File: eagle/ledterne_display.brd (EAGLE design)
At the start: 15 x 15 mm, 5 parts

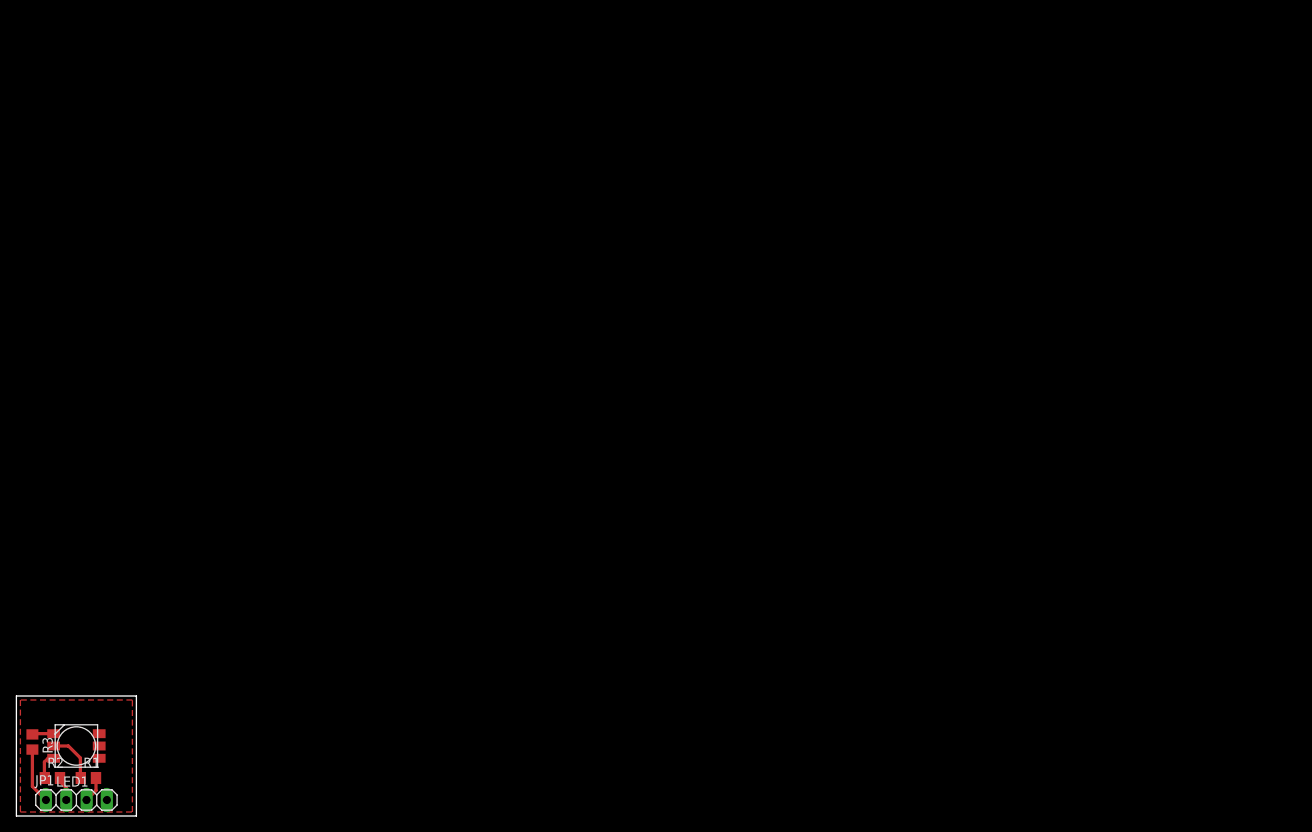
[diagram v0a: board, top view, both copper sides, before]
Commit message: Add layout versions for printing a complete Eurocard board
The display board also has Yo's entirely unrelated layout on the
same Eurocard.
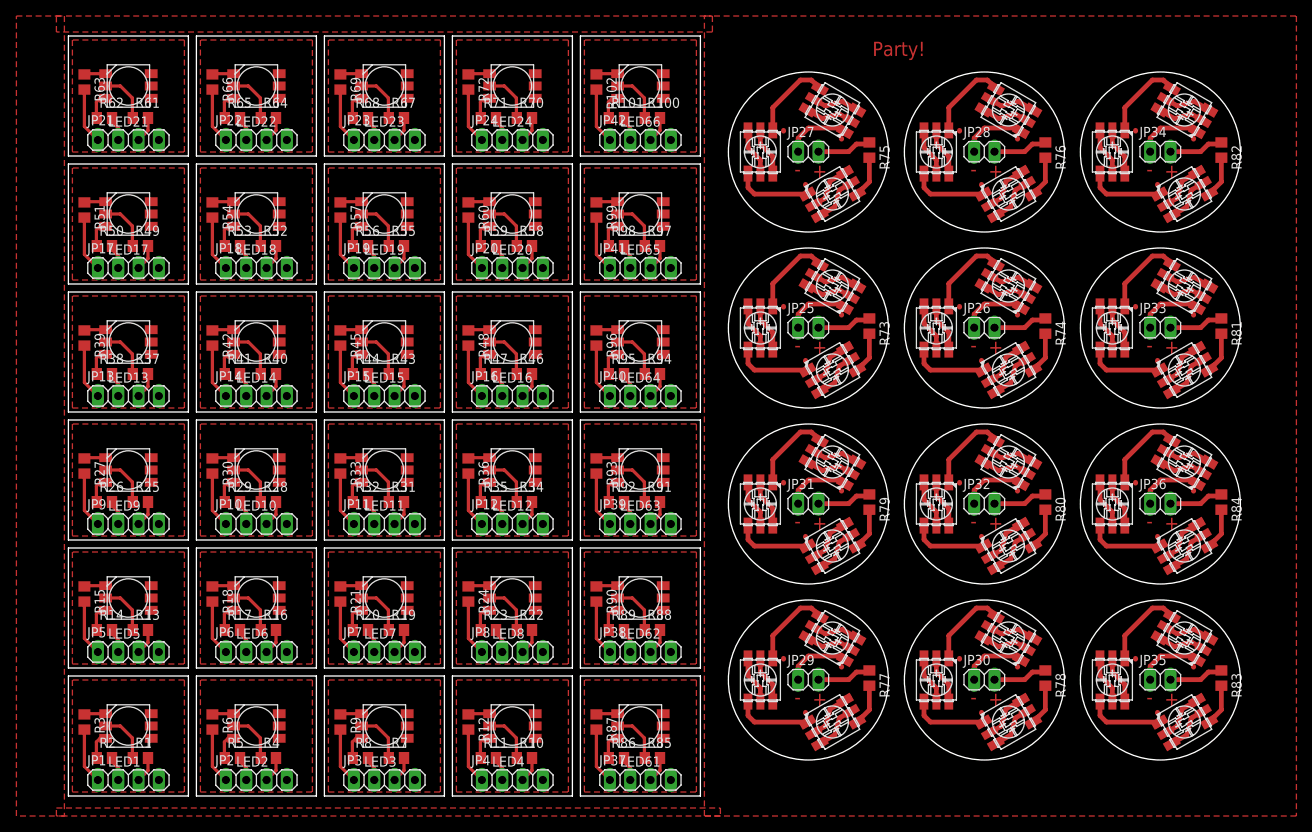
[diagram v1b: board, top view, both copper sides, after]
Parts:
- added JP10, JP11, JP12, JP13, JP14, JP15, JP16, JP17, JP18, JP19, JP2, JP20, JP21, JP22, JP23, JP24, JP3, JP37, JP38, JP39, JP4, JP40, JP41, JP42, JP5, JP6, JP7, JP8, JP9: (no value), pinhead:1X04
- added JP25, JP26, JP27, JP28, JP29, JP30, JP31, JP32, JP33, JP34, JP35, JP36: (no value), pinhead:1X02
- added LED10, LED11, LED12, LED13, LED14, LED15, LED16, LED17, LED18, LED19, LED2, LED20, LED21, LED22, LED23, LED24, LED3, LED4, LED5, LED6, LED61, LED62, LED63, LED64, LED65, LED66, LED7, LED8, LED9: RGB-5252, led-rgb:SMD_5252
- added LED25, LED26, LED27, LED28, LED29, LED30, LED31, LED32, LED33, LED34, LED35, LED36, LED37, LED38, LED39, LED40, LED41, LED42, LED43, LED44, LED45, LED46, LED47, LED48, LED49, LED50, LED51, LED52, LED53, LED54, LED55, LED56, LED57, LED58, LED59, LED60: LUCKYLIGHT-R5050, led:PLCC-6
- added R10, R100, R101, R102, R11, R12, R13, R14, R15, R16, R17, R18, R19, R20, R21, R22, R23, R24, R25, R26, R27, R28, R29, R30, R31, R32, R33, R34, R35, R36, R37, R38, R39, R4, R40, R41, R42, R43, R44, R45, R46, R47, R48, R49, R5, R50, R51, R52, R53, R54, R55, R56, R57, R58, R59, R6, R60, R61, R62, R63, R64, R65, R66, R67, R68, R69, R7, R70, R71, R72, R8, R85, R86, R87, R88, R89, R9, R90, R91, R92, R93, R94, R95, R96, R97, R98, R99: (no value), resistor:R0805
- added R73, R74, R75, R76, R77, R78, R79, R80, R81, R82, R83, R84: 225, rcl:R0805
- moved JP1 6.96 mm to (14.0, 4.50)
- moved LED1 6.96 mm to (14.0, 11.2)
- moved R1 6.96 mm to (15.5, 7.25)
- moved R2 6.96 mm to (11.0, 7.25)
- moved R3 6.96 mm to (8.50, 11.8)
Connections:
- new net 22,5V: JP25.2, R73.1
- new net 22,5V1: JP26.2, R74.1
- new net 22,5V10: JP35.2, R83.1
- new net 22,5V11: JP36.2, R84.1
- new net 22,5V2: JP27.2, R75.1
- new net 22,5V3: JP28.2, R76.1
- new net 22,5V4: JP29.2, R77.1
- new net 22,5V5: JP30.2, R78.1
- new net 22,5V6: JP31.2, R79.1
- new net 22,5V7: JP32.2, R80.1
- new net 22,5V8: JP33.2, R81.1
- new net 22,5V9: JP34.2, R82.1
- new net GND1: JP2.4, LED2.P4, LED2.P5, LED2.P6
- new net GND10: JP11.4, LED11.P4, LED11.P5, LED11.P6
- new net GND11: JP12.4, LED12.P4, LED12.P5, LED12.P6
- new net GND12: JP13.4, LED13.P4, LED13.P5, LED13.P6
- new net GND13: JP14.4, LED14.P4, LED14.P5, LED14.P6
- new net GND14: JP15.4, LED15.P4, LED15.P5, LED15.P6
- new net GND15: JP16.4, LED16.P4, LED16.P5, LED16.P6
- new net GND16: JP17.4, LED17.P4, LED17.P5, LED17.P6
- new net GND17: JP18.4, LED18.P4, LED18.P5, LED18.P6
- new net GND18: JP19.4, LED19.P4, LED19.P5, LED19.P6
- new net GND19: JP20.4, LED20.P4, LED20.P5, LED20.P6
- new net GND2: JP3.4, LED3.P4, LED3.P5, LED3.P6
- new net GND20: JP21.4, LED21.P4, LED21.P5, LED21.P6
- new net GND21: JP22.4, LED22.P4, LED22.P5, LED22.P6
- new net GND22: JP23.4, LED23.P4, LED23.P5, LED23.P6
- new net GND23: JP24.4, LED24.P4, LED24.P5, LED24.P6
- new net GND24: JP25.1, LED27.P$1
- new net GND25: JP26.1, LED30.P$1
- new net GND26: JP27.1, LED33.P$1
- new net GND27: JP28.1, LED36.P$1
- new net GND28: JP29.1, LED39.P$1
- new net GND29: JP30.1, LED42.P$1
- new net GND3: JP4.4, LED4.P4, LED4.P5, LED4.P6
- new net GND30: JP31.1, LED45.P$1
- new net GND31: JP32.1, LED48.P$1
- new net GND32: JP33.1, LED51.P$1
- new net GND33: JP34.1, LED54.P$1
- new net GND34: JP35.1, LED57.P$1
- new net GND35: JP36.1, LED60.P$1
- new net GND36: JP37.4, LED61.P4, LED61.P5, LED61.P6
- new net GND37: JP38.4, LED62.P4, LED62.P5, LED62.P6
- new net GND38: JP39.4, LED63.P4, LED63.P5, LED63.P6
- new net GND39: JP40.4, LED64.P4, LED64.P5, LED64.P6
- new net GND4: JP5.4, LED5.P4, LED5.P5, LED5.P6
- new net GND40: JP41.4, LED65.P4, LED65.P5, LED65.P6
- new net GND41: JP42.4, LED66.P4, LED66.P5, LED66.P6
- new net GND5: JP6.4, LED6.P4, LED6.P5, LED6.P6
- new net GND6: JP7.4, LED7.P4, LED7.P5, LED7.P6
- new net GND7: JP8.4, LED8.P4, LED8.P5, LED8.P6
- new net GND8: JP9.4, LED9.P4, LED9.P5, LED9.P6
- new net GND9: JP10.4, LED10.P4, LED10.P5, LED10.P6
- new net LED_B1: JP2.1, R6.2
- new net LED_B10: JP11.1, R33.2
- new net LED_B11: JP12.1, R36.2
- new net LED_B12: JP13.1, R39.2
- new net LED_B13: JP14.1, R42.2
- new net LED_B14: JP15.1, R45.2
- new net LED_B15: JP16.1, R48.2
- new net LED_B16: JP17.1, R51.2
- new net LED_B17: JP18.1, R54.2
- new net LED_B18: JP19.1, R57.2
- new net LED_B19: JP20.1, R60.2
- new net LED_B2: JP3.1, R9.2
- new net LED_B20: JP21.1, R63.2
- new net LED_B21: JP22.1, R66.2
- new net LED_B22: JP23.1, R69.2
- new net LED_B23: JP24.1, R72.2
- new net LED_B24: JP37.1, R87.2
- new net LED_B25: JP38.1, R90.2
- new net LED_B26: JP39.1, R93.2
- new net LED_B27: JP40.1, R96.2
- new net LED_B28: JP41.1, R99.2
- new net LED_B29: JP42.1, R102.2
- new net LED_B3: JP4.1, R12.2
- new net LED_B4: JP5.1, R15.2
- new net LED_B5: JP6.1, R18.2
- new net LED_B6: JP7.1, R21.2
- new net LED_B7: JP8.1, R24.2
- new net LED_B8: JP9.1, R27.2
- new net LED_B9: JP10.1, R30.2
- new net LED_G1: JP2.2, R5.2
- new net LED_G10: JP11.2, R32.2
- new net LED_G11: JP12.2, R35.2
- new net LED_G12: JP13.2, R38.2
- new net LED_G13: JP14.2, R41.2
- new net LED_G14: JP15.2, R44.2
- new net LED_G15: JP16.2, R47.2
- new net LED_G16: JP17.2, R50.2
- new net LED_G17: JP18.2, R53.2
- new net LED_G18: JP19.2, R56.2
- new net LED_G19: JP20.2, R59.2
- new net LED_G2: JP3.2, R8.2
- new net LED_G20: JP21.2, R62.2
- new net LED_G21: JP22.2, R65.2
- new net LED_G22: JP23.2, R68.2
- new net LED_G23: JP24.2, R71.2
- new net LED_G24: JP37.2, R86.2
- new net LED_G25: JP38.2, R89.2
- new net LED_G26: JP39.2, R92.2
- new net LED_G27: JP40.2, R95.2
- new net LED_G28: JP41.2, R98.2
- new net LED_G29: JP42.2, R101.2
- new net LED_G3: JP4.2, R11.2
- new net LED_G4: JP5.2, R14.2
- new net LED_G5: JP6.2, R17.2
- new net LED_G6: JP7.2, R20.2
- new net LED_G7: JP8.2, R23.2
- new net LED_G8: JP9.2, R26.2
- new net LED_G9: JP10.2, R29.2
- new net LED_R1: JP2.3, R4.2
- new net LED_R10: JP11.3, R31.2
- new net LED_R11: JP12.3, R34.2
- new net LED_R12: JP13.3, R37.2
- new net LED_R13: JP14.3, R40.2
- new net LED_R14: JP15.3, R43.2
- new net LED_R15: JP16.3, R46.2
- new net LED_R16: JP17.3, R49.2
- new net LED_R17: JP18.3, R52.2
- new net LED_R18: JP19.3, R55.2
- new net LED_R19: JP20.3, R58.2
- new net LED_R2: JP3.3, R7.2
- new net LED_R20: JP21.3, R61.2
- new net LED_R21: JP22.3, R64.2
- new net LED_R22: JP23.3, R67.2
- new net LED_R23: JP24.3, R70.2
- new net LED_R24: JP37.3, R85.2
- new net LED_R25: JP38.3, R88.2
- new net LED_R26: JP39.3, R91.2
- new net LED_R27: JP40.3, R94.2
- new net LED_R28: JP41.3, R97.2
- new net LED_R29: JP42.3, R100.2
- new net LED_R3: JP4.3, R10.2
- new net LED_R4: JP5.3, R13.2
- new net LED_R5: JP6.3, R16.2
- new net LED_R6: JP7.3, R19.2
- new net LED_R7: JP8.3, R22.2
- new net LED_R8: JP9.3, R25.2
- new net LED_R9: JP10.3, R28.2
- new net N$10: LED4.P2, R10.1
- new net N$100: LED33.P$3, LED33.P$5
- new net N$101: LED32.P$1, LED33.P$4
- new net N$102: LED32.P$2, LED32.P$6
- new net N$103: LED32.P$3, LED32.P$5
- new net N$104: LED31.P$1, LED32.P$4
- new net N$105: LED31.P$2, LED31.P$6
- new net N$106: LED31.P$3, LED31.P$5
- new net N$107: LED31.P$4, R75.2
- new net N$11: LED4.P3, R11.1
- new net N$112: LED36.P$2, LED36.P$6
- new net N$113: LED36.P$3, LED36.P$5
- new net N$114: LED35.P$1, LED36.P$4
- new net N$115: LED35.P$2, LED35.P$6
- new net N$116: LED35.P$3, LED35.P$5
- new net N$117: LED34.P$1, LED35.P$4
- new net N$118: LED34.P$2, LED34.P$6
- new net N$119: LED34.P$3, LED34.P$5
- new net N$12: LED4.P1, R12.1
- new net N$120: LED34.P$4, R76.2
- new net N$125: LED39.P$2, LED39.P$6
- new net N$126: LED39.P$3, LED39.P$5
- new net N$127: LED38.P$1, LED39.P$4
- new net N$128: LED38.P$2, LED38.P$6
- new net N$129: LED38.P$3, LED38.P$5
- new net N$13: LED5.P2, R13.1
- new net N$130: LED37.P$1, LED38.P$4
- new net N$131: LED37.P$2, LED37.P$6
- new net N$132: LED37.P$3, LED37.P$5
- new net N$133: LED37.P$4, R77.2
- new net N$138: LED42.P$2, LED42.P$6
- new net N$139: LED42.P$3, LED42.P$5
- new net N$14: LED5.P3, R14.1
- new net N$140: LED41.P$1, LED42.P$4
- new net N$141: LED41.P$2, LED41.P$6
- new net N$142: LED41.P$3, LED41.P$5
- new net N$143: LED40.P$1, LED41.P$4
- new net N$144: LED40.P$2, LED40.P$6
- new net N$145: LED40.P$3, LED40.P$5
- new net N$146: LED40.P$4, R78.2
- new net N$15: LED5.P1, R15.1
- new net N$151: LED45.P$2, LED45.P$6
- new net N$152: LED45.P$3, LED45.P$5
- new net N$153: LED44.P$1, LED45.P$4
- new net N$154: LED44.P$2, LED44.P$6
- new net N$155: LED44.P$3, LED44.P$5
- new net N$156: LED43.P$1, LED44.P$4
- new net N$157: LED43.P$2, LED43.P$6
- new net N$158: LED43.P$3, LED43.P$5
- new net N$159: LED43.P$4, R79.2
- new net N$16: LED6.P2, R16.1
- new net N$164: LED48.P$2, LED48.P$6
- new net N$165: LED48.P$3, LED48.P$5
- new net N$166: LED47.P$1, LED48.P$4
- new net N$167: LED47.P$2, LED47.P$6
- new net N$168: LED47.P$3, LED47.P$5
- new net N$169: LED46.P$1, LED47.P$4
- new net N$17: LED6.P3, R17.1
- new net N$170: LED46.P$2, LED46.P$6
- new net N$171: LED46.P$3, LED46.P$5
- new net N$172: LED46.P$4, R80.2
- new net N$177: LED51.P$2, LED51.P$6
- new net N$178: LED51.P$3, LED51.P$5
- new net N$179: LED50.P$1, LED51.P$4
- new net N$18: LED6.P1, R18.1
- new net N$180: LED50.P$2, LED50.P$6
- new net N$181: LED50.P$3, LED50.P$5
- new net N$182: LED49.P$1, LED50.P$4
- new net N$183: LED49.P$2, LED49.P$6
- new net N$184: LED49.P$3, LED49.P$5
- new net N$185: LED49.P$4, R81.2
- new net N$19: LED7.P2, R19.1
- new net N$190: LED54.P$2, LED54.P$6
- new net N$191: LED54.P$3, LED54.P$5
- new net N$192: LED53.P$1, LED54.P$4
- new net N$193: LED53.P$2, LED53.P$6
- new net N$194: LED53.P$3, LED53.P$5
- new net N$195: LED52.P$1, LED53.P$4
- new net N$196: LED52.P$2, LED52.P$6
- new net N$197: LED52.P$3, LED52.P$5
- new net N$198: LED52.P$4, R82.2
- new net N$20: LED7.P3, R20.1
- new net N$203: LED57.P$2, LED57.P$6
- new net N$204: LED57.P$3, LED57.P$5
- new net N$205: LED56.P$1, LED57.P$4
- new net N$206: LED56.P$2, LED56.P$6
- new net N$207: LED56.P$3, LED56.P$5
- new net N$208: LED55.P$1, LED56.P$4
- new net N$209: LED55.P$2, LED55.P$6
- new net N$21: LED7.P1, R21.1
- new net N$210: LED55.P$3, LED55.P$5
- new net N$211: LED55.P$4, R83.2
- new net N$216: LED60.P$2, LED60.P$6
- new net N$217: LED60.P$3, LED60.P$5
- new net N$218: LED59.P$1, LED60.P$4
- new net N$219: LED59.P$2, LED59.P$6
- new net N$22: LED8.P2, R22.1
- new net N$220: LED59.P$3, LED59.P$5
- new net N$221: LED58.P$1, LED59.P$4
- new net N$222: LED58.P$2, LED58.P$6
- new net N$223: LED58.P$3, LED58.P$5
- new net N$224: LED58.P$4, R84.2
- new net N$229: LED61.P2, R85.1
- new net N$23: LED8.P3, R23.1
- new net N$230: LED61.P3, R86.1
- new net N$231: LED61.P1, R87.1
- new net N$232: LED62.P2, R88.1
- new net N$233: LED62.P3, R89.1
- new net N$234: LED62.P1, R90.1
- new net N$235: LED63.P2, R91.1
- new net N$236: LED63.P3, R92.1
- new net N$237: LED63.P1, R93.1
- new net N$238: LED64.P2, R94.1
- new net N$239: LED64.P3, R95.1
- new net N$24: LED8.P1, R24.1
- new net N$240: LED64.P1, R96.1
- new net N$241: LED65.P2, R97.1
- new net N$242: LED65.P3, R98.1
- new net N$243: LED65.P1, R99.1
- new net N$244: LED66.P2, R100.1
- new net N$245: LED66.P3, R101.1
- new net N$246: LED66.P1, R102.1
- new net N$25: LED9.P2, R25.1
- new net N$26: LED9.P3, R26.1
- new net N$27: LED9.P1, R27.1
- new net N$28: LED10.P2, R28.1
- new net N$29: LED10.P3, R29.1
- new net N$30: LED10.P1, R30.1
- new net N$31: LED11.P2, R31.1
- new net N$32: LED11.P3, R32.1
- new net N$33: LED11.P1, R33.1
- new net N$34: LED12.P2, R34.1
- new net N$35: LED12.P3, R35.1
- new net N$36: LED12.P1, R36.1
- new net N$37: LED13.P2, R37.1
- new net N$38: LED13.P3, R38.1
- new net N$39: LED13.P1, R39.1
- new net N$4: LED2.P2, R4.1
- new net N$40: LED14.P2, R40.1
- new net N$41: LED14.P3, R41.1
- new net N$42: LED14.P1, R42.1
- new net N$43: LED15.P2, R43.1
- new net N$44: LED15.P3, R44.1
- new net N$45: LED15.P1, R45.1
- new net N$46: LED16.P2, R46.1
- new net N$47: LED16.P3, R47.1
- new net N$48: LED16.P1, R48.1
- new net N$49: LED17.P2, R49.1
- new net N$5: LED2.P3, R5.1
- new net N$50: LED17.P3, R50.1
- new net N$51: LED17.P1, R51.1
- new net N$52: LED18.P2, R52.1
- new net N$53: LED18.P3, R53.1
- new net N$54: LED18.P1, R54.1
- new net N$55: LED19.P2, R55.1
- new net N$56: LED19.P3, R56.1
- new net N$57: LED19.P1, R57.1
- new net N$58: LED20.P2, R58.1
- new net N$59: LED20.P3, R59.1
- new net N$6: LED2.P1, R6.1
- new net N$60: LED20.P1, R60.1
- new net N$61: LED21.P2, R61.1
- new net N$62: LED21.P3, R62.1
- new net N$63: LED21.P1, R63.1
- new net N$64: LED22.P2, R64.1
- new net N$65: LED22.P3, R65.1
- new net N$66: LED22.P1, R66.1
- new net N$67: LED23.P2, R67.1
- new net N$68: LED23.P3, R68.1
- new net N$69: LED23.P1, R69.1
- new net N$7: LED3.P2, R7.1
- new net N$70: LED24.P2, R70.1
- new net N$71: LED24.P3, R71.1
- new net N$72: LED24.P1, R72.1
- new net N$73: LED27.P$2, LED27.P$6
- new net N$74: LED27.P$3, LED27.P$5
- new net N$75: LED26.P$1, LED27.P$4
- new net N$76: LED26.P$2, LED26.P$6
- new net N$77: LED26.P$3, LED26.P$5
- new net N$78: LED25.P$1, LED26.P$4
- new net N$79: LED25.P$2, LED25.P$6
- new net N$8: LED3.P3, R8.1
- new net N$80: LED25.P$3, LED25.P$5
- new net N$81: LED25.P$4, R73.2
- new net N$86: LED30.P$2, LED30.P$6
- new net N$87: LED30.P$3, LED30.P$5
- new net N$88: LED29.P$1, LED30.P$4
- new net N$89: LED29.P$2, LED29.P$6
- new net N$9: LED3.P1, R9.1
- new net N$90: LED29.P$3, LED29.P$5
- new net N$91: LED28.P$1, LED29.P$4
- new net N$92: LED28.P$2, LED28.P$6
- new net N$93: LED28.P$3, LED28.P$5
- new net N$94: LED28.P$4, R74.2
- new net N$99: LED33.P$2, LED33.P$6
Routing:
- net N$88: track 0.00 -> 10.6 mm
- net N$75: track 0.00 -> 10.6 mm
- net N$114: track 0.00 -> 10.6 mm
- net N$101: track 0.00 -> 10.6 mm
- net N$140: track 0.00 -> 10.6 mm
- net N$127: track 0.00 -> 10.6 mm
- net N$192: track 0.00 -> 10.6 mm
- net N$179: track 0.00 -> 10.6 mm
- net N$205: track 0.00 -> 10.6 mm
- net N$166: track 0.00 -> 10.6 mm
- net N$153: track 0.00 -> 10.6 mm
- net N$218: track 0.00 -> 10.6 mm
- net N$208: track 0.00 -> 9.52 mm
- net N$221: track 0.00 -> 9.52 mm
- net N$182: track 0.00 -> 9.52 mm
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- added copper zone on layer 1, net GND1
- added copper zone on layer 1, net GND10
- added copper zone on layer 1, net GND11
- added copper zone on layer 1, net GND12
- added copper zone on layer 1, net GND13
- added copper zone on layer 1, net GND14
- added copper zone on layer 1, net GND15
- added copper zone on layer 1, net GND16
- added copper zone on layer 1, net GND17
- added copper zone on layer 1, net GND18
- added copper zone on layer 1, net GND19
- added copper zone on layer 1, net GND2
- added copper zone on layer 1, net GND20
- added copper zone on layer 1, net GND21
- added copper zone on layer 1, net GND22
- added copper zone on layer 1, net GND23
- added copper zone on layer 1, net GND3
- added copper zone on layer 1, net GND36
- added copper zone on layer 1, net GND37
- added copper zone on layer 1, net GND38
- added copper zone on layer 1, net GND39
- added copper zone on layer 1, net GND4
- added copper zone on layer 1, net GND40
- added copper zone on layer 1, net GND41
- added copper zone on layer 1, net GND5
- added copper zone on layer 1, net GND6
- added copper zone on layer 1, net GND7
- added copper zone on layer 1, net GND8
- added copper zone on layer 1, net GND9
- added copper zone on layer 1, net S$1
- added copper zone on layer 1, net S$2
- added copper zone on layer 1, net S$3
- added copper zone on layer 1, net S$4
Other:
- board size 15 x 15 mm -> 146.5 x 95 mm
- board text added: "+"
- board text added: "-"
- board text added: "Party!"
- board text added: "•"
